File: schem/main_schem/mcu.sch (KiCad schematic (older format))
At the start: 0 parts

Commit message: Vdd and ethernet conns to mcu
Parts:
- added C? (x6): 0.1uF, symbol CP
- added C?: 1uF, symbol CP
- added R?: 2.26k 1%, symbol R
- added U?: PIC18F97J60, symbol PIC18F97J60
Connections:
- new net ETH_BUS1: U?.73 (TPIN-)
- new net ETH_BUS2: U?.74 (TPIN+)
- new net ETH_BUS3: U?.78 (TP0UT+)
- new net ETH_BUS4: U?.77 (TPOUT-)
- new net MCLR: U?.13 (MCLR)
- new net RBIAS: R?.2, U?.80 (RBIAS)
- new net VDD: C?.1, C?.1, C?.1, C?.1, C?.1, C?.1, C?.1, U?.16 (VDDCORE/VCAP), U?.17 (VDD), U?.37 (VDD), U?.59 (Vdd), U?.62 (Vdd), U?.86 (Vdd)
- new net VSS: C?.2, C?.2, C?.2, C?.2, C?.2, C?.2, C?.2, R?.1, U?.15 (VSS), U?.36 (Vss), U?.40 (Vss), U?.60 (Vss), U?.65 (Vss), U?.85 (Vss)
- no-connect marks 0 -> 1

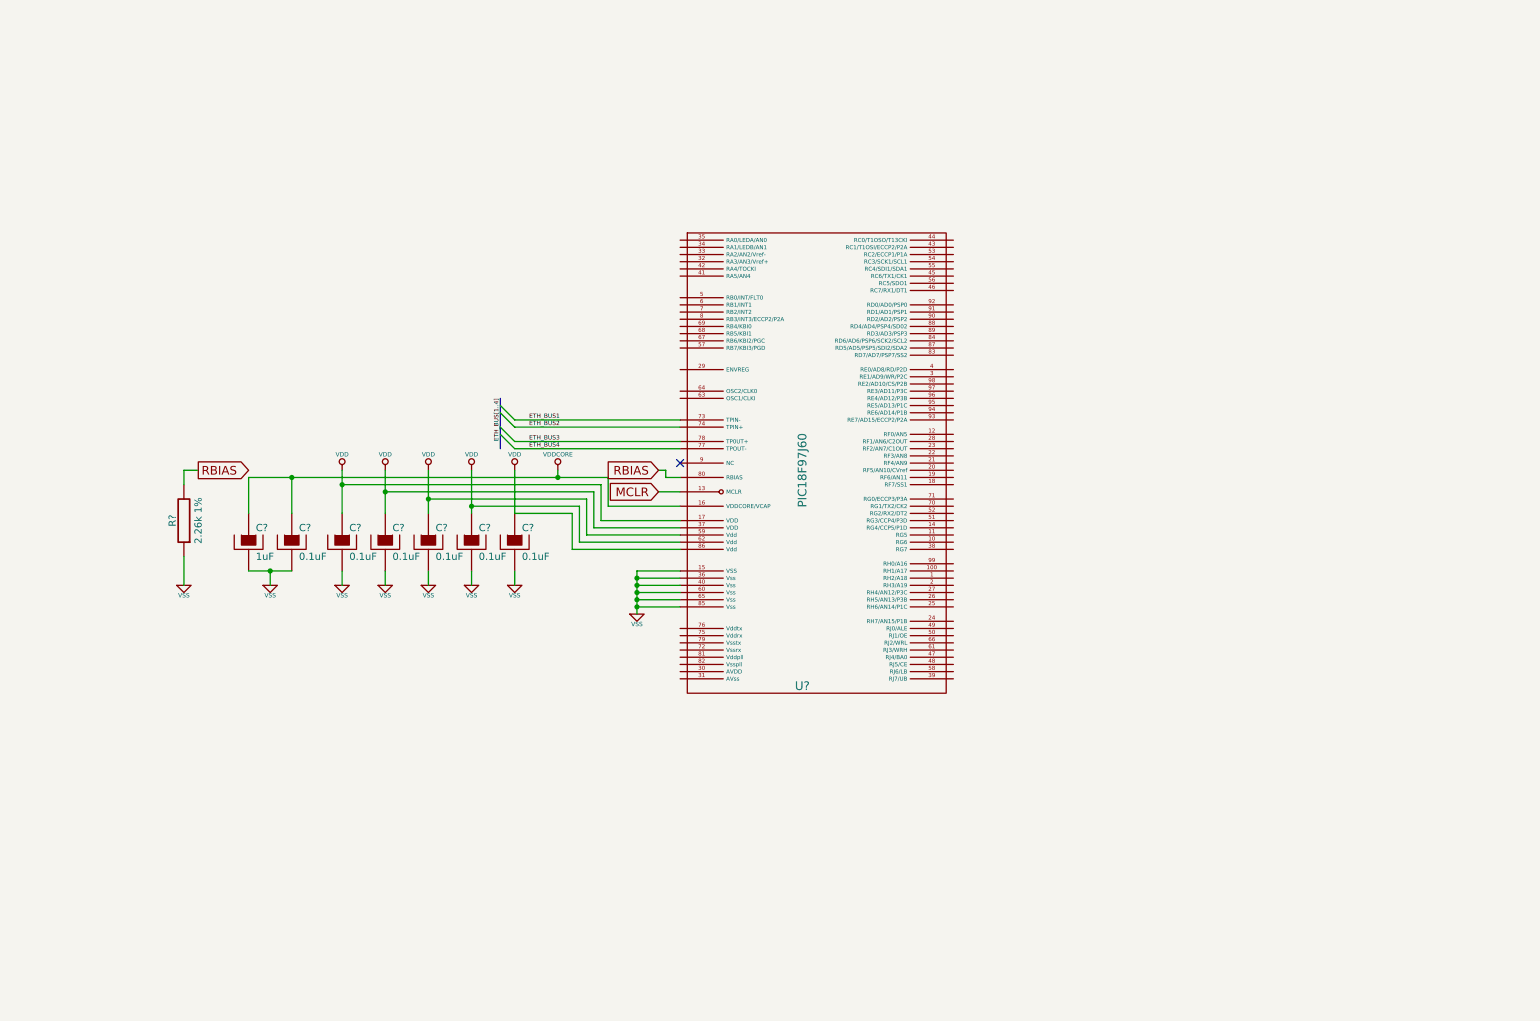
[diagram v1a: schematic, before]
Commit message: Crystal and Debug for MCU
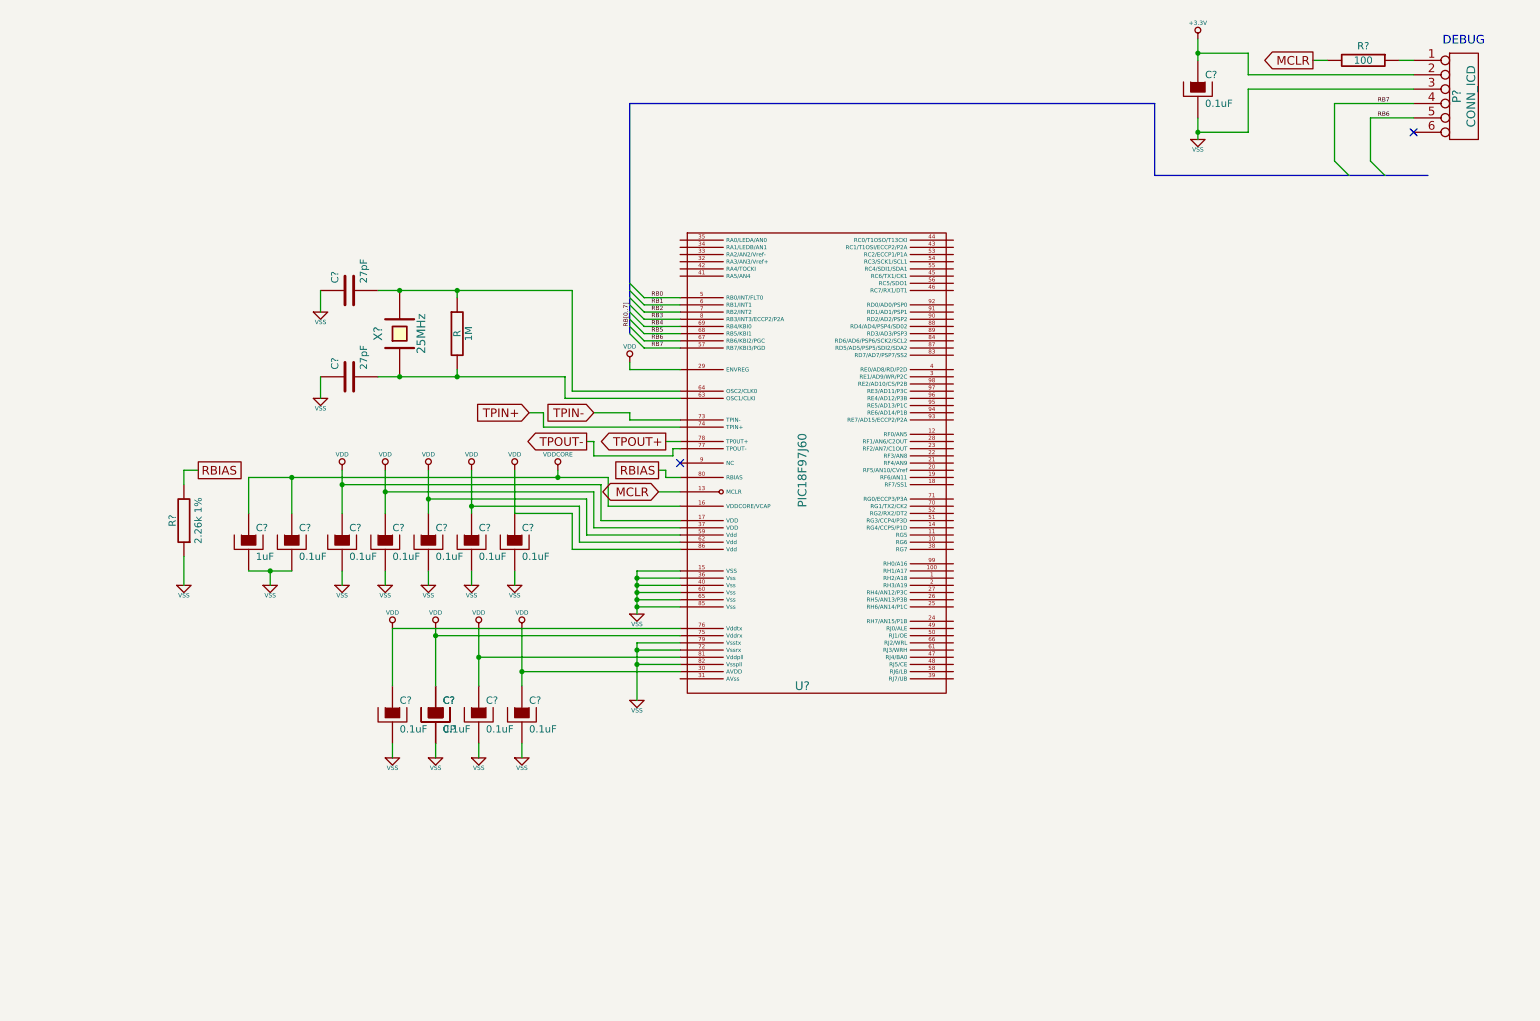
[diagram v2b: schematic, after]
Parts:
- added 1M: R, symbol R
- added C? (x5): 0.1uF, symbol CP
- added C?: CP, symbol CP
- added C? (x2): 27pF, symbol C
- added P?: CONN_ICD, symbol CONN_6
- added R?: 100, symbol R
- added X?: 25MHz, symbol CRYSTAL
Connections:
- net MCLR: now also R?.2
- net VDD: now also U?.29 (ENVREG), U?.30 (AVDD), U?.75 (Vddrx), U?.76 (Vddtx), U?.81 (Vddpll), C?.1, C?.1, C?.1, C?.1, C?.1
- net VSS: now also U?.72 (Vssrx), U?.79 (Vsstx), U?.82 (Vsspll), C?.1, C?.1, C?.2, C?.2, C?.2, C?.2, C?.2, C?.2, P?.3
- net RB0: now reaches U?.5 (RB0/INT/FLT0)
- net RB7: now reaches U?.57 (RB7/KBI3/PGD)
- net RB7: now also P?.4
- net RB1: now reaches U?.6 (RB1/INT1)
- net at U?.63 (OSC1/CLKI): now also 1M.2, C?.2, X?.1
- net at U?.64 (OSC2/CLK0): now also 1M.1, C?.2, X?.2
- net RB6: now reaches U?.67 (RB6/KBI2/PGC)
- net RB6: now also P?.5
- net RB5: now reaches U?.68 (RB5/KBI1)
- net RB4: now reaches U?.69 (RB4/KBI0)
- net RB2: now reaches U?.7 (RB2/INT2)
- net RB3: now reaches U?.8 (RB3/INT3/ECCP2/P2A)
- net ETH_BUS1 renamed TPIN-
- net ETH_BUS2 renamed TPIN+
- net ETH_BUS3 renamed TPOUT+
- net ETH_BUS4 renamed TPOUT-
- new net: P?.1, R?.1
- new net +3.3V: C?.1, P?.2
- no-connect marks 1 -> 2
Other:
- note added: "DEBUG"

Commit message: Switches and LEDs
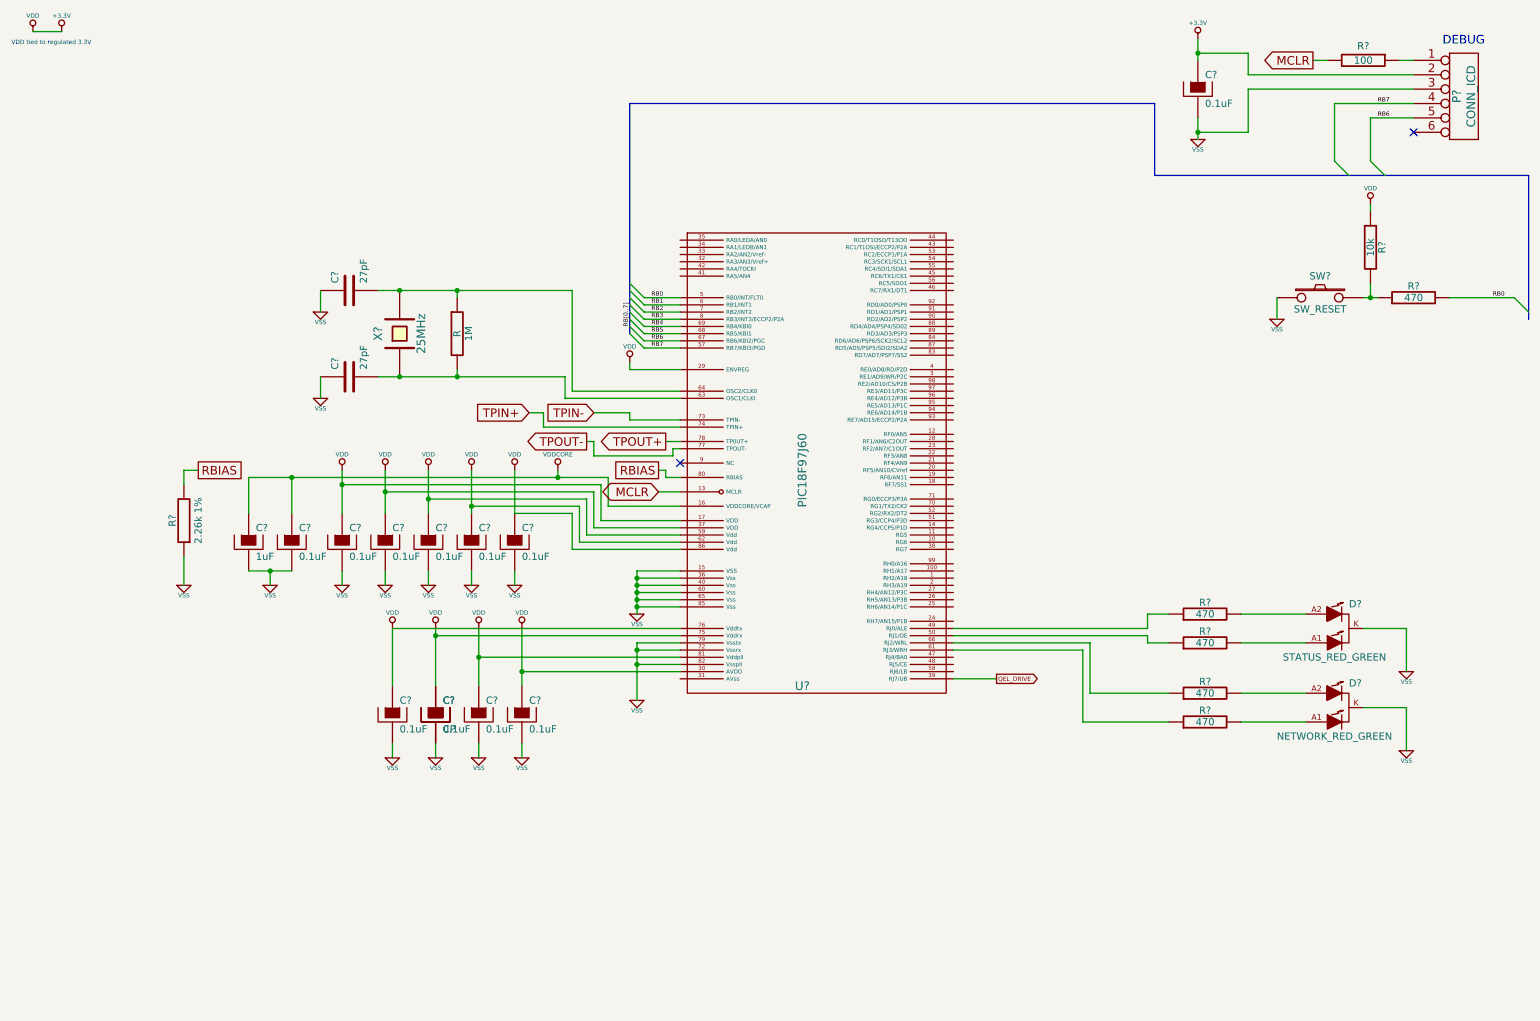
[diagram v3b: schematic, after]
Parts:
- added D?: STATUS_RED_GREEN, symbol DOUBLE_LED
- added D?: NETWORK_RED_GREEN, symbol DOUBLE_LED
- added R? (x5): 470, symbol R
- added R?: 10k, symbol R
- added SW?: SW_RESET, symbol SW_PUSH
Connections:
- net VDD is gone; now on net +3.3V: C?.1, C?.1, C?.1, C?.1, C?.1, C?.1, C?.1, C?.1, C?.1, C?.1, C?.1, C?.1, U?.16 (VDDCORE/VCAP), U?.17 (VDD), U?.29 (ENVREG), U?.30 (AVDD), U?.37 (VDD), U?.59 (Vdd), U?.62 (Vdd), U?.75 (Vddrx), U?.76 (Vddtx), U?.81 (Vddpll), U?.86 (Vdd)
- net +3.3V: now also R?.1
- net RB0: now also R?.2
- net VSS: now also D?.K, D?.K, SW?.1
- net QEL_DRIVE: now reaches U?.39 (RJ7/UB)
- net at U?.49 (RJ0/ALE): now also R?.1
- net at U?.50 (RJ1/OE): now also R?.1
- net at U?.61 (RJ3/WRH): now also R?.1
- net at U?.66 (RJ2/WRL): now also R?.1
- new net: D?.A2, R?.2 (x2)
- new net: D?.A1, R?.2 (x2)
- new net: R?.1, R?.2, SW?.2
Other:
- note added: "VDD tied to regulated 3.3V"
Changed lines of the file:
@@
-EESchema Schematic File Version 2  date 9/29/2012 9:59:06 AM
+EESchema Schematic File Version 2  date 9/29/2012 10:23:31 AM
 LIBS:power
 LIBS:device
@@
 Rev "1"
 Comp "ECE 402 Senior Design, Ingersoll Rand Group"
-Comment1 "Everything except for PIC18 IC block Copyright (c) Brock Anderson 2012"
-Comment2 "All rights reserved.  Not for commercial use."
+Comment1 "Layout (not graphics) Copyright (c) Brock Anderson 2012.  All rights reserved."
+Comment2 ""
 Comment3 ""
 Comment4 ""
 $EndDescr
+Wire Wire Line
+	10000 1950 10000 2000
+Wire Wire Line
+	9950 2600 10050 2600
+Wire Bus Line
+	11100 2750 11100 1750
+Wire Wire Line
+	9350 2600 9350 2750
+Wire Bus Line
+	11100 1750 8500 1750
+Wire Wire Line
+	10250 5200 10250 4900
+Wire Wire Line
+	10250 4900 9950 4900
+Wire Wire Line
+	8600 5550 8000 5550
+Wire Wire Line
+	8000 5550 8000 5050
+Wire Wire Line
+	8000 5050 7100 5050
+Wire Wire Line
+	7100 4950 8450 4950
+Wire Wire Line
+	8450 4950 8450 5000
+Wire Wire Line
+	8450 5000 8600 5000
+Wire Wire Line
+	8600 4800 8450 4800
+Wire Wire Line
+	8450 4800 8450 4900
+Wire Wire Line
+	8450 4900 7100 4900
+Wire Wire Line
+	9100 4800 9550 4800
+Wire Wire Line
+	9100 5350 9550 5350
 Connection ~ 3650 3150
 Wire Wire Line
@@
 Wire Bus Line
 	8500 1250 8500 1750
-Wire Bus Line
-	8500 1750 10400 1750
 Wire Wire Line
 	9750 1650 9750 1250
@@
 	4400 3300 5200 3300
 Connection ~ 3250 3150
+Wire Wire Line
+	700  750  900  750
+Wire Wire Line
+	9100 5550 9550 5550
+Wire Wire Line
+	9100 5000 9550 5000
+Wire Wire Line
+	7100 5000 8050 5000
+Wire Wire Line
+	8050 5000 8050 5350
+Wire Wire Line
+	8050 5350 8600 5350
+Wire Wire Line
+	7100 5250 7400 5250
+Wire Wire Line
+	9950 5450 10250 5450
+Wire Wire Line
+	10250 5450 10250 5750
+Wire Wire Line
+	11000 2600 10550 2600
+Wire Wire Line
+	10000 2500 10000 2600
+Connection ~ 10000 2600
+$Comp
+L VDD #PWR?
+U 1 1 506711C2
+P 10000 1950
+F 0 "#PWR?" H 10000 2050 30  0001 C CNN
+F 1 "VDD" H 10000 2060 30  0000 C CNN
+	1    10000 1950
+	1    0    0    -1
+$EndComp
+$Comp
+L R R?
+U 1 1 506711A8
+P 10000 2250
+F 0 "R?" V 10080 2250 50  0000 C CNN
+F 1 "10k" V 10000 2250 50  0000 C CNN
+	1    10000 2250
+	1    0    0    -1
+$EndComp
+Entry Wire Line
+	11000 2600 11100 2700
+$Comp
+L R R?
+U 1 1 5067115F
+P 10300 2600
+F 0 "R?" V 10380 2600 50  0000 C CNN
+F 1 "470" V 10300 2600 50  0000 C CNN
+	1    10300 2600
+	0    -1   -1   0
+$EndComp
+$Comp
+L VSS #PWR?
+U 1 1 5067114D
+P 9350 2750
+F 0 "#PWR?" H 9350 2750 30  0001 C CNN
+F 1 "VSS" H 9350 2680 30  0000 C CNN
+	1    9350 2750
+	1    0    0    -1
+$EndComp
+Text Label 10850 2600 0    30   ~ 0
+RB0
+$Comp
+L SW_PUSH SW?
+U 1 1 5067111F
+P 9650 2600
+F 0 "SW?" H 9650 2750 50  0000 C CNN
+F 1 "SW_RESET" H 9650 2520 50  0000 C CNN
+	1    9650 2600
+	1    0    0    -1
+$EndComp
+$Comp
+L VSS #PWR?
+U 1 1 506710A1
+P 10250 5200
+F 0 "#PWR?" H 10250 5200 30  0001 C CNN
+F 1 "VSS" H 10250 5130 30  0000 C CNN
+	1    10250 5200
+	1    0    0    -1
+$EndComp
+$Comp
+L VSS #PWR?
+U 1 1 5067109D
+P 10250 5750
+F 0 "#PWR?" H 10250 5750 30  0001 C CNN
+F 1 "VSS" H 10250 5680 30  0000 C CNN
+	1    10250 5750
+	1    0    0    -1
+$EndComp
+Text GLabel 7400 5250 2    30   Output ~ 0
+QEL_DRIVE
+$Comp
+L R R?
+U 1 1 50670F86
+P 8850 5550
+F 0 "R?" V 8930 5550 50  0000 C CNN
+F 1 "470" V 8850 5550 50  0000 C CNN
+	1    8850 5550
+	0    -1   -1   0
+$EndComp
+$Comp
+L R R?
+U 1 1 50670F80
+P 8850 5350
+F 0 "R?" V 8930 5350 50  0000 C CNN
+F 1 "470" V 8850 5350 50  0000 C CNN
+	1    8850 5350
+	0    -1   -1   0
+$EndComp
+$Comp
+L DOUBLE_LED D?
+U 1 1 50670F68
+P 9750 5450
+F 0 "D?" H 9850 5620 50  0000 L CNN
+F 1 "NETWORK_RED_GREEN" H 9750 5250 50  0000 C CNN
+	1    9750 5450
+	1    0    0    -1
+$EndComp
+$Comp
+L DOUBLE_LED D?
+U 1 1 50670F61
+P 9750 4900
+F 0 "D?" H 9850 5070 50  0000 L CNN
+F 1 "STATUS_RED_GREEN" H 9750 4700 50  0000 C CNN
+	1    9750 4900
+	1    0    0    -1
+$EndComp
+$Comp
+L R R?
+U 1 1 50670EF7
+P 8850 5000
+F 0 "R?" V 8930 5000 50  0000 C CNN
+F 1 "470" V 8850 5000 50  0000 C CNN
+	1    8850 5000
+	0    -1   -1   0
+$EndComp
+$Comp
+L R R?
+U 1 1 50670EEE
+P 8850 4800
+F 0 "R?" V 8930 4800 50  0000 C CNN
+F 1 "470" V 8850 4800 50  0000 C CNN
+	1    8850 4800
+	0    -1   -1   0
+$EndComp
+Text Notes 550  850  0    30   ~ 0
+VDD tied to regulated 3.3V
+$Comp
+L +3.3V #PWR?
+U 1 1 50670E40
+P 900 750
+F 0 "#PWR?" H 900 710 30  0001 C CNN
+F 1 "+3.3V" H 900 860 30  0000 C CNN
+	1    900  750
+	1    0    0    -1
+$EndComp
+$Comp
+L VDD #PWR?
+U 1 1 50670E3A
+P 700 750
+F 0 "#PWR?" H 700 850 30  0001 C CNN
+F 1 "VDD" H 700 860 30  0000 C CNN
+	1    700  750
+	1    0    0    -1
+$EndComp
 $Comp
 L R 1M

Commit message: Link status lights for RJ45 jack
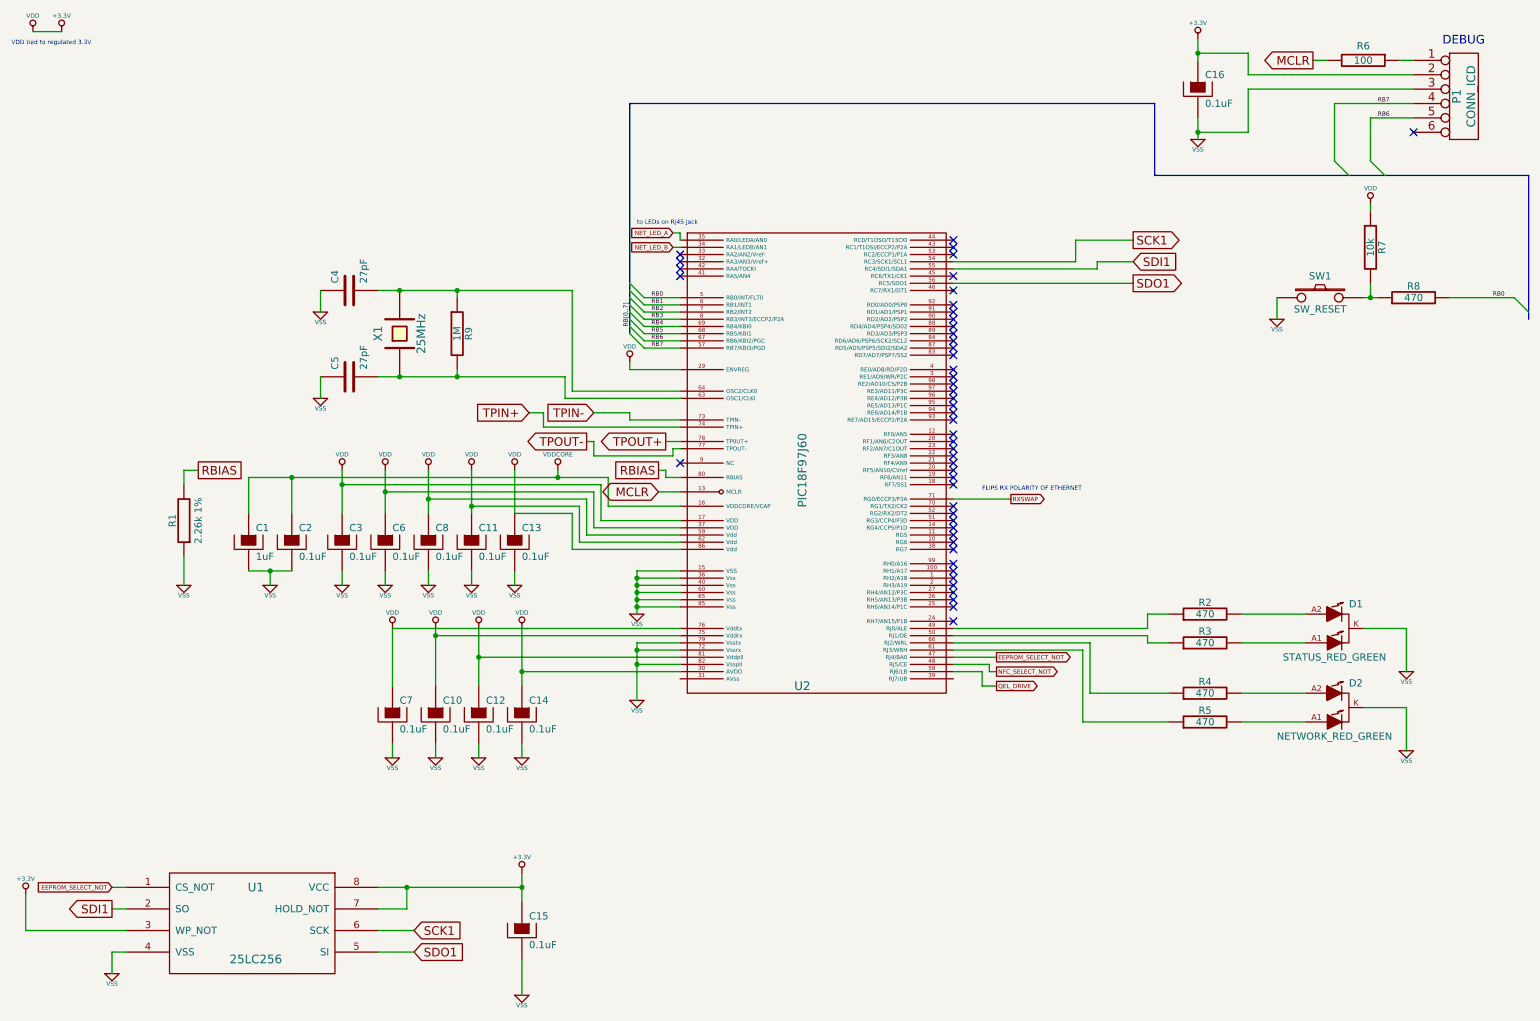
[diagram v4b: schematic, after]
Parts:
- removed C?: CP, symbol CP
- added C15: 0.1uF, symbol CP
- added U1: 25LC256, symbol 25LC256
- R9: renamed from 1M; value R -> 1M
- gave numbers to parts that had none: 28
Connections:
- net +3.3V: now also C15.1, U1.3 (WP_NOT), U1.7 (HOLD_NOT), U1.8 (VCC)
- net QEL_DRIVE: now also U2.58 (RJ6/LB); no longer U2.39 (RJ7/UB)
- net VSS: now also C15.2, U1.4 (VSS)
- net NET_LED_B: now reaches U2.34 (RA1/LEDB/AN1)
- net NET_LED_A: now reaches U2.35 (RA0/LEDA/AN0)
- net EEPROM_SELECT_NOT: now reaches U2.47 (RJ4/BA0)
- net EEPROM_SELECT_NOT: now also U1.1 (CS_NOT)
- net NFC_SELECT_NOT: now reaches U2.48 (RJ5/CE)
- net SCK1: now reaches U2.54 (RC3/SCK1/SCL1)
- net SCK1: now also U1.6 (SCK)
- net SDI1: now reaches U2.55 (RC4/SDI1/SDA1)
- net SDI1: now also U1.2 (SO)
- net SDO1: now reaches U2.56 (RC5/SDO1)
- net SDO1: now also U1.5 (SI)
- net RXSWAP: now reaches U2.71 (RG0/ECCP3/P3A)
- no-connect marks 2 -> 50
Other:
- note added: "FLIPS RX POLARITY OF ETHERNET"
- note added: "to LEDs on RJ45 Jack"
